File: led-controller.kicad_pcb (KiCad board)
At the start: 2 copper layers, 33 x 57 mm, 35 parts, among them J1 Screw_Terminal_01x02, J2 Screw_Terminal_01x04, J3 Conn_01x04, J4 Misc1, J5 Misc2, SW1 Reset, SW2 Flash, U1 NCP1117-3.3_SOT223, U2 ESP-12F, U3 SN74LVC1T45DBV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

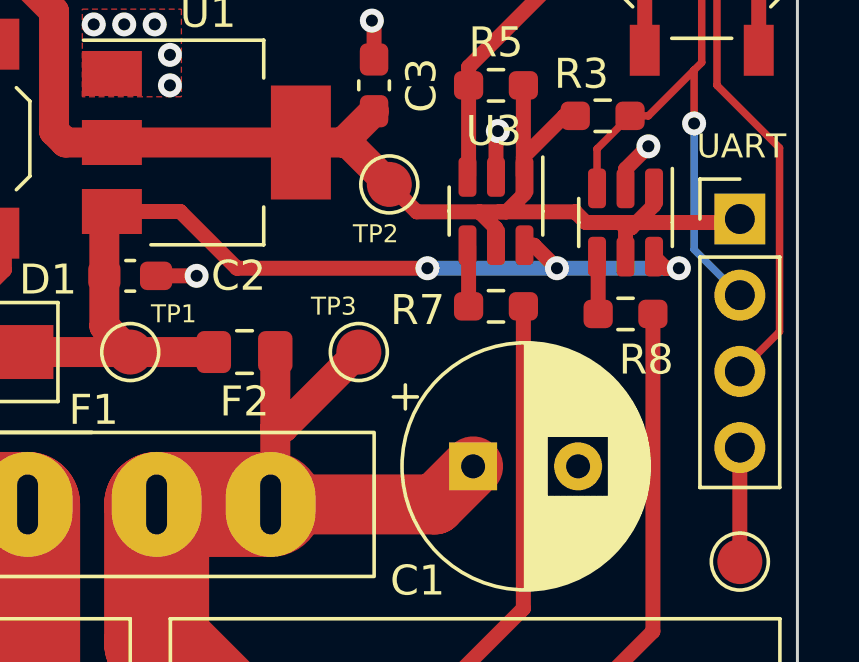
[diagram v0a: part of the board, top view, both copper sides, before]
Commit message: Created case for device. Added gerber files for PCB manufacturing.
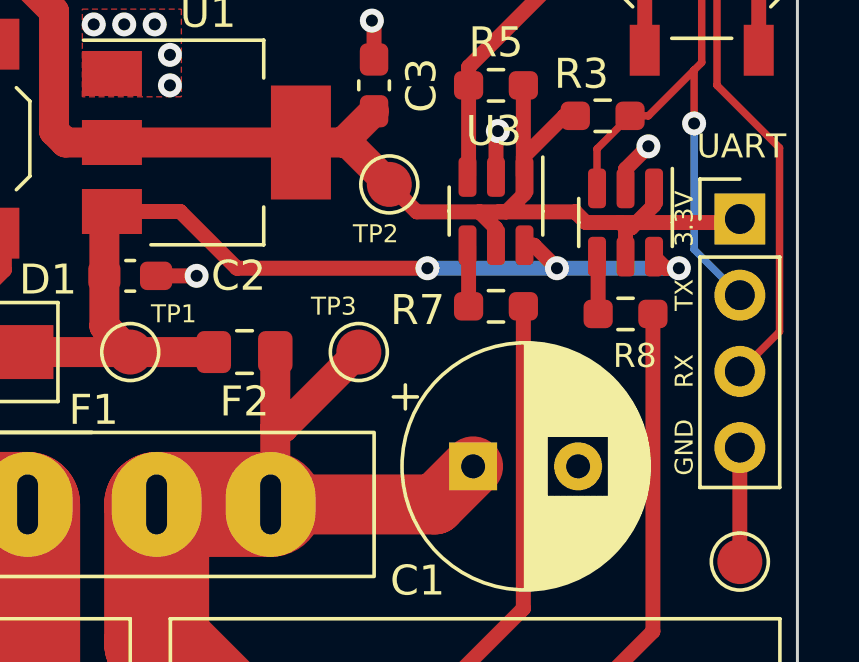
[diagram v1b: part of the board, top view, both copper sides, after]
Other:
- board text added: "3.3V"
- board text added: "RX"
- board text added: "TX"
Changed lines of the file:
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@@
       (layerselection 0x00010fc_ffffffff)
       (disableapertmacros false)
-      (usegerberextensions false)
+      (usegerberextensions true)
       (usegerberattributes true)
-      (usegerberadvancedattributes true)
-      (creategerberjobfile true)
+      (usegerberadvancedattributes false)
+      (creategerberjobfile false)
       (svguseinch false)
       (svgprecision 6)
@@
       (psa4output false)
       (plotreference true)
-      (plotvalue true)
+      (plotvalue false)
       (plotinvisibletext false)
       (sketchpadsonfab false)
-      (subtractmaskfromsilk false)
+      (subtractmaskfromsilk true)
       (outputformat 1)
       (mirror false)
-      (drillshape 1)
+      (drillshape 0)
       (scaleselection 1)
-      (outputdirectory "")
+      (outputdirectory "fabric/")
     )
   )
@@
     (property "Sheetname" "")
     (attr smd)
-    (fp_text reference "R8" (at -0.689 -1.524) (layer "F.SilkS")
-      (effects (font (size 1 1) (thickness 0.15)))
+    (fp_text reference "R8" (at -0.308 -1.397) (layer "F.SilkS")
+      (effects (font (size 0.8 0.8) (thickness 0.15)))
     )
     (fp_text value "100" (at 0 1.43) (layer "F.Fab")
@@
     (fp_line (start -1 -0.6) (end 1 -0.6) (layer "F.Fab") (width 0.1))
     (fp_line (start 1 0.6) (end -1 0.6) (layer "F.Fab") (width 0.1))
-    (pad "1" smd roundrect (at -1.025 0 180) (size 1.15 1.4) (layers "F.Cu" "F.Paste" "F.Mask") (roundrect_rratio 0.217391)
+    (pad "1" smd roundrect (at -1.025 0 180) (size 1.15 1.4) (layers "F.Cu" "F.Paste" "F.Mask") (roundrect_rratio 0.2173913043)
       (net 1 "+5P") (pintype "passive"))
-    (pad "2" smd roundrect (at 1.025 0 180) (size 1.15 1.4) (layers "F.Cu" "F.Paste" "F.Mask") (roundrect_rratio 0.217391)
+    (pad "2" smd roundrect (at 1.025 0 180) (size 1.15 1.4) (layers "F.Cu" "F.Paste" "F.Mask") (roundrect_rratio 0.2173913043)
       (net 3 "+5V") (pintype "passive"))
     (model "${KICAD6_3DMODEL_DIR}/Fuse.3dshapes/Fuse_0805_2012Metric.wrl"
@@
     (effects (font (size 1 1) (thickness 0.15)))
   )
+  (gr_text "3.3V" (at 117.729 102.235 90) (layer "F.SilkS")
+    (effects (font (size 0.6 0.6) (thickness 0.15)))
+  )
+  (gr_text "TX" (at 117.729 104.775 90) (layer "F.SilkS")
+    (effects (font (size 0.6 0.6) (thickness 0.15)))
+  )
   (gr_text "GND" (at 118.364 124.46) (layer "F.SilkS")
     (effects (font (size 1 1) (thickness 0.15)))
   )
+  (gr_text "GND" (at 117.729 109.855 90) (layer "F.SilkS")
+    (effects (font (size 0.6 0.6) (thickness 0.15)))
+  )
+  (gr_text "RX\n" (at 117.729 107.315 90) (layer "F.SilkS")
+    (effects (font (size 0.6 0.6) (thickness 0.15)))
+  )
   (gr_text "D16" (at 90.424 81.661) (layer "F.SilkS")
